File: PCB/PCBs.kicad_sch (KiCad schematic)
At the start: 1 part, among them U1 ADS1299IPAGR

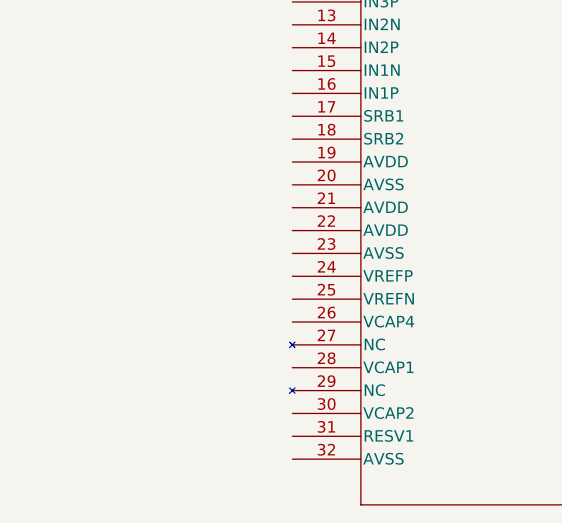
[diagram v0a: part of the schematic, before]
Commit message: adding vcaps
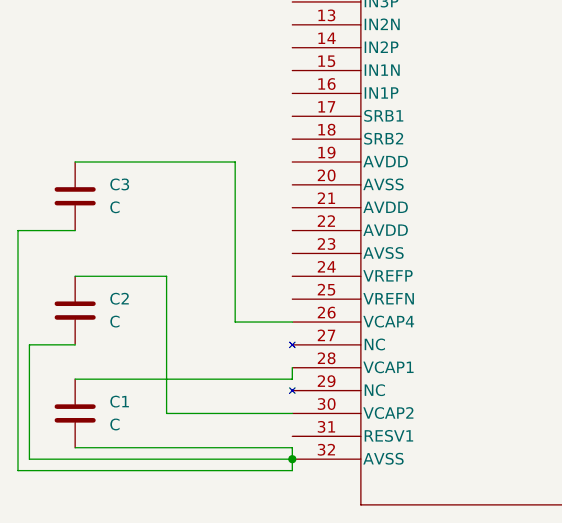
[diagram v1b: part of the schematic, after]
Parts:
- added C1, C2, C3: C, symbol Device:C
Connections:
- net at U1.26 (VCAP4): now also C3.1
- net at U1.28 (VCAP1): now also C1.1
- net at U1.30 (VCAP2): now also C2.1
- net at U1.32 (AVSS): now also C1.2, C2.2, C3.2

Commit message: moving vcaps
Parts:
- added C4: 0.1µF, symbol Device:C
- added C5: 1µF, symbol Device:C
- added U2: ESP32-WROOM-32, ESP32-WROOM-32:MODULE_ESP32-WROOM-32, symbol custom_lib:ESP32-WROOM-32
- C1: value C -> 100µF
- C2, C3: value C -> 1µF
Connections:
- net at U1.26 (VCAP4): now also C5.1; no longer C3.1
- net AVSS: now reaches C1.2, C2.2
- net AVSS: now also C3.1, C4.1, C5.2; no longer C3.2, U1.32 (AVSS)
- net at U1.55 (VCAP3): now also C3.2, C4.2
- new net: U2.1 (GND), U2.15 (GND), U2.38 (GND), U2.39_1 (GND), U2.39_10 (GND), U2.39_11 (GND), U2.39_12 (GND), U2.39_13 (GND), U2.39_14 (GND), U2.39_15 (GND), U2.39_16 (GND), U2.39_17 (GND), U2.39_18 (GND), U2.39_19 (GND), U2.39_2 (GND), U2.39_20 (GND), U2.39_21 (GND), U2.39_3 (GND), U2.39_4 (GND), U2.39_5 (GND), U2.39_6 (GND), U2.39_7 (GND), U2.39_8 (GND), U2.39_9 (GND)

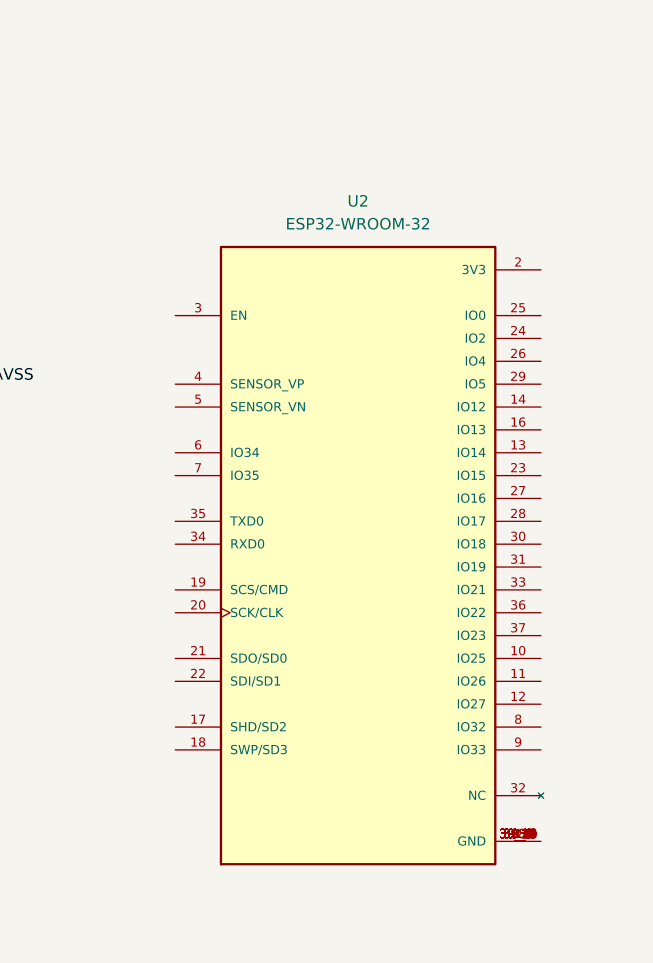
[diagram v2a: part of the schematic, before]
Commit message: esp32 to pi pico
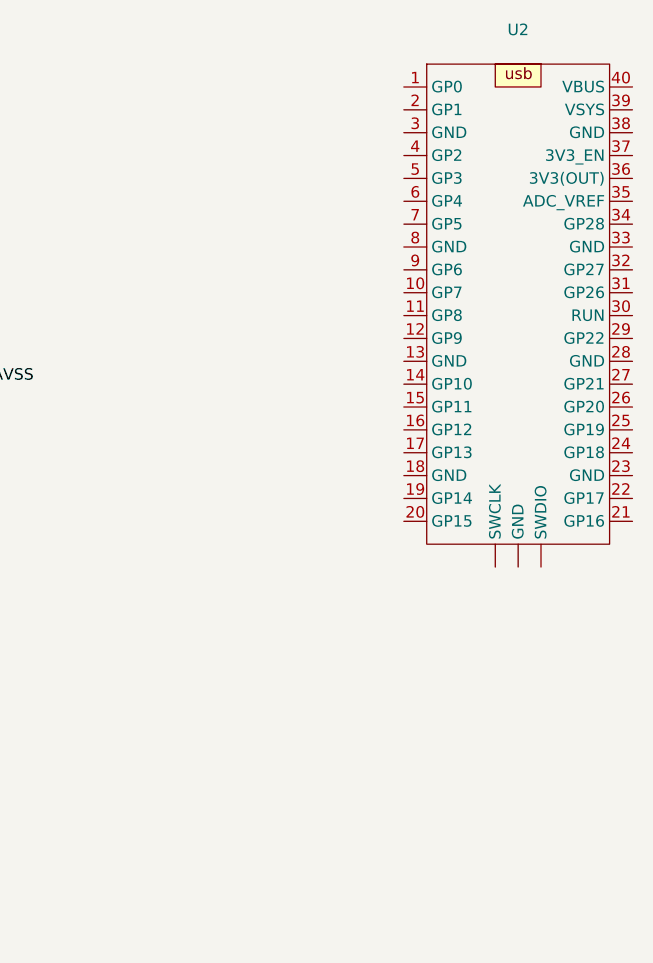
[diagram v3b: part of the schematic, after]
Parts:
- removed U2: ESP32-WROOM-32, ESP32-WROOM-32:MODULE_ESP32-WROOM-32, symbol custom_lib:ESP32-WROOM-32
- added U2: ~, Library:Raspberry_pi_pico, symbol custom_lib:pi_pico
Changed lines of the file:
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@@
 	)
 	(symbol
-		(lib_id "custom_lib:ESP32-WROOM-32")
-		(at 251.46 104.14 0)
+		(lib_id "custom_lib:pi_pico")
+		(at 269.24 45.72 0)
 		(unit 1)
 		(exclude_from_sim no)
@@
 		(fields_autoplaced yes)
 		(property "Reference" "U2"
-			(at 251.46 63.5 0)
+			(at 269.24 44.45 0)
 			(effects
 				(font
@@
 			)
 		)
-		(property "Value" "ESP32-WROOM-32"
-			(at 251.46 66.04 0)
+		(property "Value" "~"
+			(at 269.24 46.99 0)
 			(effects
 				(font
@@
 			)
 		)
-		(property "Footprint" "ESP32-WROOM-32:MODULE_ESP32-WROOM-32"
-			(at 251.46 104.14 0)
+		(property "Footprint" "Library:Raspberry_pi_pico"
+			(at 269.24 45.72 0)
 			(effects
 				(font
 					(size 1.27 1.27)
 				)
-				(justify bottom)
 				(hide yes)
 			)
 		)
 		(property "Datasheet" ""
-			(at 251.46 104.14 0)
+			(at 269.24 45.72 0)
 			(effects
 				(font
@@
 		)
 		(property "Description" ""
-			(at 251.46 104.14 0)
+			(at 269.24 45.72 0)
 			(effects
 				(font
@@
 			)
 		)
-		(property "MF" "Espressif Systems"
-			(at 251.46 104.14 0)
-			(effects
-				(font
-					(size 1.27 1.27)
-				)
-				(justify bottom)
-				(hide yes)
-			)
+		(pin "10"
 		)
-		(property "MAXIMUM_PACKAGE_HEIGHT" "3.2 mm"
-			(at 251.46 104.14 0)
-			(effects
-				(font
-					(size 1.27 1.27)
-				)
-				(justify bottom)
-				(hide yes)
-			)
+		(pin "22"
 		)
-		(property "Package" "None"
-			(at 251.46 104.14 0)
-			(effects
-				(font
-					(size 1.27 1.27)
-				)
-				(justify bottom)
-				(hide yes)
-			)
+		(pin "23"
 		)
-		(property "Price" "None"
-			(at 251.46 104.14 0)
-			(effects
-				(font
-					(size 1.27 1.27)
-				)
-				(justify bottom)
-				(hide yes)
-			)
+		(pin "34"
 		)
-		(property "Check_prices" "https://www.snapeda.com/parts/ESP32-WROOM-32/Espressif+Systems/view-part/?ref=eda"
-			(at 251.46 104.14 0)
-			(effects
-				(font
-					(size 1.27 1.27)
-				)
-				(justify bottom)
-				(hide yes)
-			)
+		(pin "26"
 		)
-		(property "STANDARD" "Manufacturer Recommendations"
-			(at 251.46 104.14 0)
-			(effects
-				(font
-					(size 1.27 1.27)
-				)
-				(justify bottom)
-				(hide yes)
-			)
+		(pin "31"
 		)
-		(property "PARTREV" "2.9"
-			(at 251.46 104.14 0)
-			(effects
-				(font
-					(size 1.27 1.27)
-				)
-				(justify bottom)
-				(hide yes)
-			)
+		(pin "20"
 		)
-		(property "SnapEDA_Link" "https://www.snapeda.com/parts/ESP32-WROOM-32/Espressif+Systems/view-part/?ref=snap"
-			(at 251.46 104.14 0)
-			(effects
-				(font
-					(size 1.27 1.27)
-				)
-				(justify bottom)
-				(hide yes)
-			)
+		(pin "16"
 		)
-		(property "MP" "ESP32-WROOM-32"
-			(at 251.46 104.14 0)
-			(effects
-				(font
-					(size 1.27 1.27)
-				)
-				(justify bottom)
-				(hide yes)
-			)
+		(pin "25"
 		)
-		(property "Description_1" "\nBluetooth, WiFi 802.11b/g/n, Bluetooth v4.2 +EDR, Class 1, 2 and 3 Transceiver Module 2.4GHz ~ 2.5GHz Antenna Not Included, U.FL Surface Mount\n"
-			(at 251.46 104.14 0)
-			(effects
-				(font
-					(size 1.27 1.27)
-				)
-				(justify bottom)
-				(hide yes)
-			)
+		(pin "24"
 		)
-		(property "Availability" "In Stock"
-			(at 251.46 104.14 0)
-			(effects
-				(font
-					(size 1.27 1.27)
-				)
-				(justify bottom)
-				(hide yes)
-			)
+		(pin "11"
 		)
-		(property "MANUFACTURER" "Espressif Systems"
-			(at 251.46 104.14 0)
-			(effects
-				(font
-					(size 1.27 1.27)
-				)
-				(justify bottom)
-				(hide yes)
-			)
+		(pin "21"
+		)
+		(pin "27"
+		)
+		(pin "29"
+		)
+		(pin "13"
+		)
+		(pin "14"
+		)
+		(pin "28"
+		)
+		(pin "3"
+		)
+		(pin "19"
+		)
+		(pin "18"
+		)
+		(pin "30"
+		)
+		(pin "32"
+		)
+		(pin "12"
+		)
+		(pin "33"
+		)
+		(pin "17"
+		)
+		(pin "15"
+		)
+		(pin "35"
+		)
+		(pin "39"
+		)
+		(pin "4"
+		)
+		(pin "37"
+		)
+		(pin ""
+		)
+		(pin ""
+		)
+		(pin "6"
 		)
 		(pin "1"
 		)
-		(pin "39_17"
-		)
-		(pin "23"
-		)
-		(pin "39_5"
-		)
-		(pin "22"
-		)
-		(pin "39_6"
-		)
-		(pin "39_3"
-		)
-		(pin "39_7"
-		)
-		(pin "39_8"
-		)
-		(pin "21"
-		)
-		(pin "39_9"
-		)
-		(pin "10"
-		)
-		(pin "13"
-		)
-		(pin "18"
-		)
-		(pin "31"
-		)
-		(pin "39_11"
-		)
-		(pin "12"
-		)
-		(pin "20"
-		)
-		(pin "34"
-		)
-		(pin "14"
-		)
-		(pin "16"
-		)
-		(pin "27"
-		)
-		(pin "32"
-		)
-		(pin "25"
-		)
-		(pin "19"
-		)
-		(pin "39_20"
-		)
-		(pin "30"
-		)
-		(pin "33"
+		(pin "7"
 		)
 		(pin "38"
 		)
-		(pin "39_10"
+		(pin "8"
 		)
-		(pin "39_12"
-		)
-		(pin "39_14"
-		)
-		(pin "2"
-		)
-		(pin "26"
-		)
-		(pin "3"
-		)
-		(pin "39_19"
-		)
-		(pin "39_21"
+		(pin ""
 		)
 		(pin "36"
-		)
-		(pin "39_16"
-		)
-		(pin "39_4"
-		)
-		(pin "17"
-		)
-		(pin "29"
-		)
-		(pin "28"
-		)
-		(pin "35"
-		)
-		(pin "11"
-		)
-		(pin "24"
-		)
-		(pin "37"
-		)
-		(pin "15"
-		)
-		(pin "39_1"
-		)
-		(pin "39_13"
-		)
-		(pin "39_15"
-		)
-		(pin "39_18"
-		)
-		(pin "39_2"
-		)
-		(pin "4"
 		)
 		(pin "5"
@@
 		(pin "9"
 		)
-		(pin "6"
+		(pin "40"
 		)
-		(pin "8"
-		)
-		(pin "7"
+		(pin "2"
 		)
 		(instances

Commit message: vref pins
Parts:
- added C6: 10µF, symbol Device:C
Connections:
- net AVSS: now also U1.25 (VREFN), C6.2
- net at U1.24 (VREFP): now also C6.1
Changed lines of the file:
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@@
 		(color 0 0 0 0)
 	)
+	(junction
+		(at 95.25 119.38)
+		(diameter 0)
+		(color 0 0 0 0)
+	)
 	(wire
 		(pts
@@
 	(wire
 		(pts
+			(xy 88.9 119.38) (xy 95.25 119.38)
+		)
+		(stroke
+			(width 0)
+			(type default)
+		)
+	)
+	(wire
+		(pts
 			(xy 91.44 137.16) (xy 95.25 137.16)
 		)
@@
 	(wire
 		(pts
+			(xy 95.25 119.38) (xy 95.25 123.19)
+		)
+		(stroke
+			(width 0)
+			(type default)
+		)
+	)
+	(wire
+		(pts
 			(xy 205.74 87.63) (xy 205.74 83.82)
 		)
@@
 	(wire
 		(pts
+			(xy 102.87 119.38) (xy 104.14 119.38)
+		)
+		(stroke
+			(width 0)
+			(type default)
+		)
+	)
+	(wire
+		(pts
 			(xy 102.87 130.81) (xy 111.76 130.81)
 		)
@@
 	(wire
 		(pts
+			(xy 104.14 120.65) (xy 111.76 120.65)
+		)
+		(stroke
+			(width 0)
+			(type default)
+		)
+	)
+	(wire
+		(pts
 			(xy 107.95 125.73) (xy 107.95 143.51)
 		)
@@
 	(wire
 		(pts
+			(xy 95.25 123.19) (xy 111.76 123.19)
+		)
+		(stroke
+			(width 0)
+			(type default)
+		)
+	)
+	(wire
+		(pts
 			(xy 91.44 143.51) (xy 91.44 137.16)
+		)
+		(stroke
+			(width 0)
+			(type default)
+		)
+	)
+	(wire
+		(pts
+			(xy 104.14 119.38) (xy 104.14 120.65)
 		)
 		(stroke
@@
 	(label "AVSS"
 		(at 210.82 83.82 0)
+		(fields_autoplaced yes)
+		(effects
+			(font
+				(size 1.27 1.27)
+			)
+			(justify left bottom)
+		)
+	)
+	(label "AVSS"
+		(at 88.9 119.38 0)
 		(fields_autoplaced yes)
 		(effects
@@
 					(unit 1)
 				)
+			)
+		)
+	)
+	(symbol
+		(lib_id "Device:C")
+		(at 99.06 119.38 270)
+		(unit 1)
+		(exclude_from_sim no)
+		(in_bom yes)
+		(on_board yes)
+		(dnp no)
+		(property "Reference" "C6"
+			(at 103.886 114.3 90)
+			(effects
+				(font
+					(size 1.27 1.27)
+				)
+			)
+		)
+		(property "Value" "10µF "
+			(at 103.886 116.84 90)
+			(effects
+				(font
+					(size 1.27 1.27)
+				)
+			)
+		)
+		(property "Footprint" ""
+			(at 95.25 120.3452 0)
+			(effects
+				(font
+					(size 1.27 1.27)
+				)
+				(hide yes)
+			)
+		)
+		(property "Datasheet" "~"
+			(at 99.06 119.38 0)
+			(effects
+				(font
+					(size 1.27 1.27)
+				)
+				(hide yes)
+			)
+		)
+		(property "Description" "Unpolarized capacitor"
+			(at 99.06 119.38 0)
+			(effects
+				(font
+					(size 1.27 1.27)
+				)
+				(hide yes)
+			)
+		)
+		(pin "1"
+		)
+		(pin "2"
+		)
+		(instances
+			(project "PCBs"
+				(path "/5beccadf-d27e-4f5e-8faf-404ef06d8def"
+					(reference "C6")
+					(unit 1)
+				)

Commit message: ads1299 symbol planning
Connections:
- net at U1.19 (AVDD): now also U1.21 (AVDD), U1.22 (AVDD)
- net at U1.54 (AVDD1): now also U1.56 (AVDD), U1.59 (AVDD)
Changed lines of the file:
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@@
+	)
+	(junction
+		(at 111.76 113.03)
+		(diameter 0)
+		(color 0 0 0 0)
 	)
 	(junction
@@
 		(color 0 0 0 0)
 	)
+	(junction
+		(at 185.42 82.55)
+		(diameter 0)
+		(color 0 0 0 0)
+	)
 	(wire
 		(pts
@@
 	(wire
 		(pts
+			(xy 111.76 113.03) (xy 111.76 115.57)
+		)
+		(stroke
+			(width 0)
+			(type default)
+		)
+	)
+	(wire
+		(pts
 			(xy 205.74 83.82) (xy 205.74 81.28)
 		)
@@
 	(wire
 		(pts
+			(xy 109.22 107.95) (xy 109.22 113.03)
+		)
+		(stroke
+			(width 0)
+			(type default)
+		)
+	)
+	(wire
+		(pts
 			(xy 88.9 119.38) (xy 95.25 119.38)
 		)
@@
 	(wire
 		(pts
+			(xy 111.76 107.95) (xy 109.22 107.95)
+		)
+		(stroke
+			(width 0)
+			(type default)
+		)
+	)
+	(wire
+		(pts
+			(xy 182.88 74.93) (xy 185.42 74.93)
+		)
+		(stroke
+			(width 0)
+			(type default)
+		)
+	)
+	(wire
+		(pts
 			(xy 199.39 81.28) (xy 205.74 81.28)
 		)
@@
 	(wire
 		(pts
+			(xy 185.42 82.55) (xy 185.42 87.63)
+		)
+		(stroke
+			(width 0)
+			(type default)
+		)
+	)
+	(wire
+		(pts
 			(xy 95.25 119.38) (xy 95.25 123.19)
 		)
@@
 	(wire
 		(pts
+			(xy 182.88 82.55) (xy 185.42 82.55)
+		)
+		(stroke
+			(width 0)
+			(type default)
+		)
+	)
+	(wire
+		(pts
 			(xy 102.87 130.81) (xy 111.76 130.81)
 		)
@@
 	(wire
 		(pts
+			(xy 109.22 113.03) (xy 111.76 113.03)
+		)
+		(stroke
+			(width 0)
+			(type default)
+		)
+	)
+	(wire
+		(pts
 			(xy 91.44 143.51) (xy 91.44 137.16)
 		)
@@
 	(wire
 		(pts
+			(xy 182.88 87.63) (xy 185.42 87.63)
+		)
+		(stroke
+			(width 0)
+			(type default)
+		)
+	)
+	(wire
+		(pts
 			(xy 111.76 135.89) (xy 106.68 135.89)
 		)
 		(stroke
+			(width 0)
+			(type default)
+		)
+	)
+	(wire
+		(pts
+			(xy 185.42 74.93) (xy 185.42 82.55)
+		)
+		(stroke

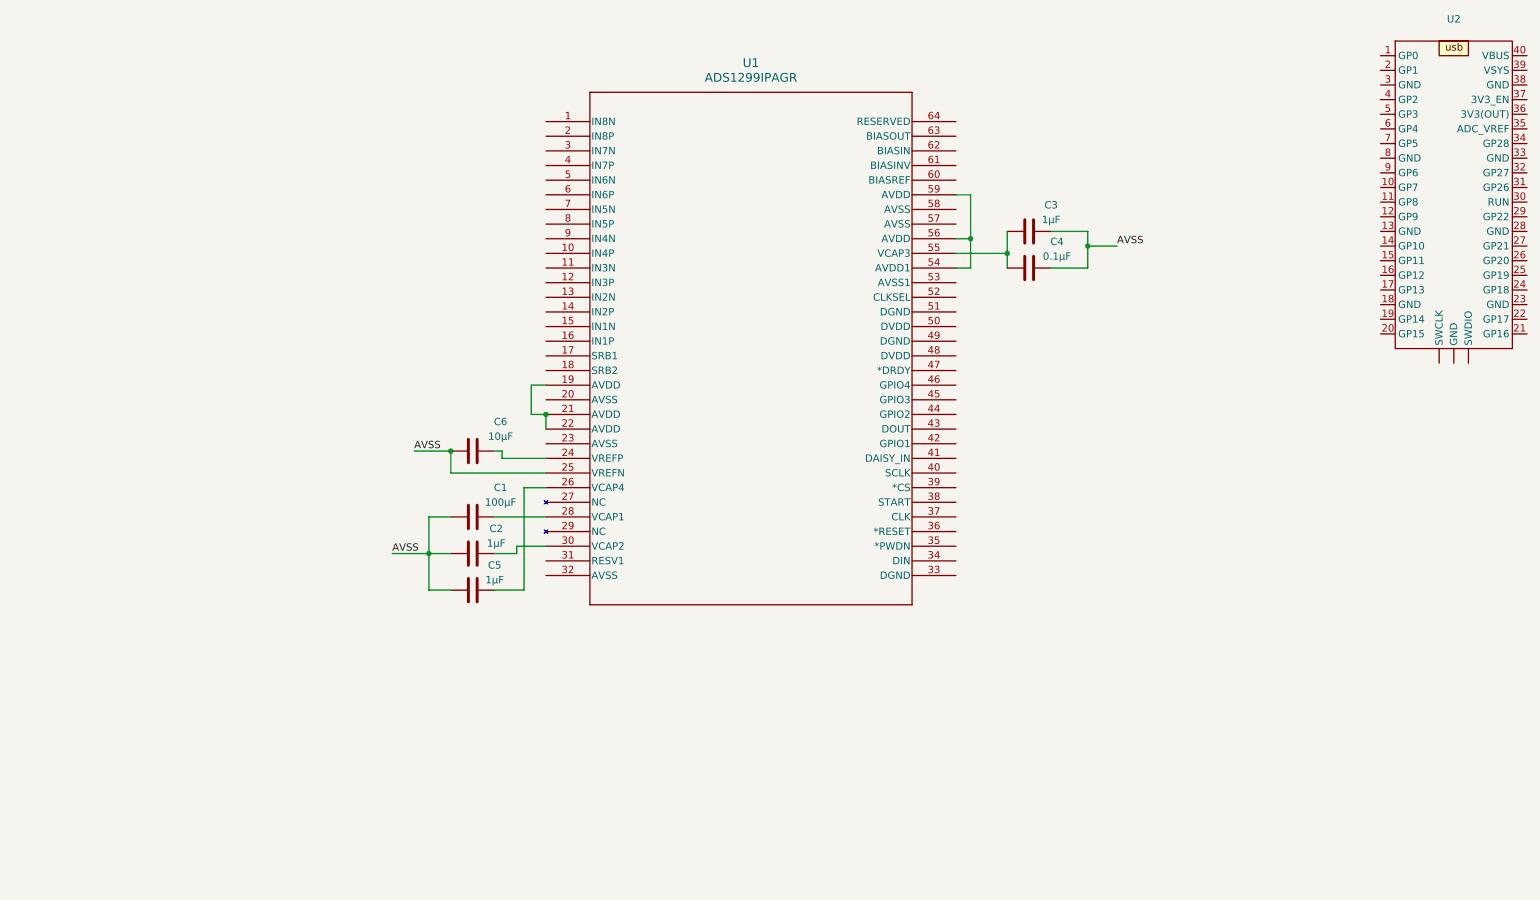
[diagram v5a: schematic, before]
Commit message: ads1299 final symbol plan
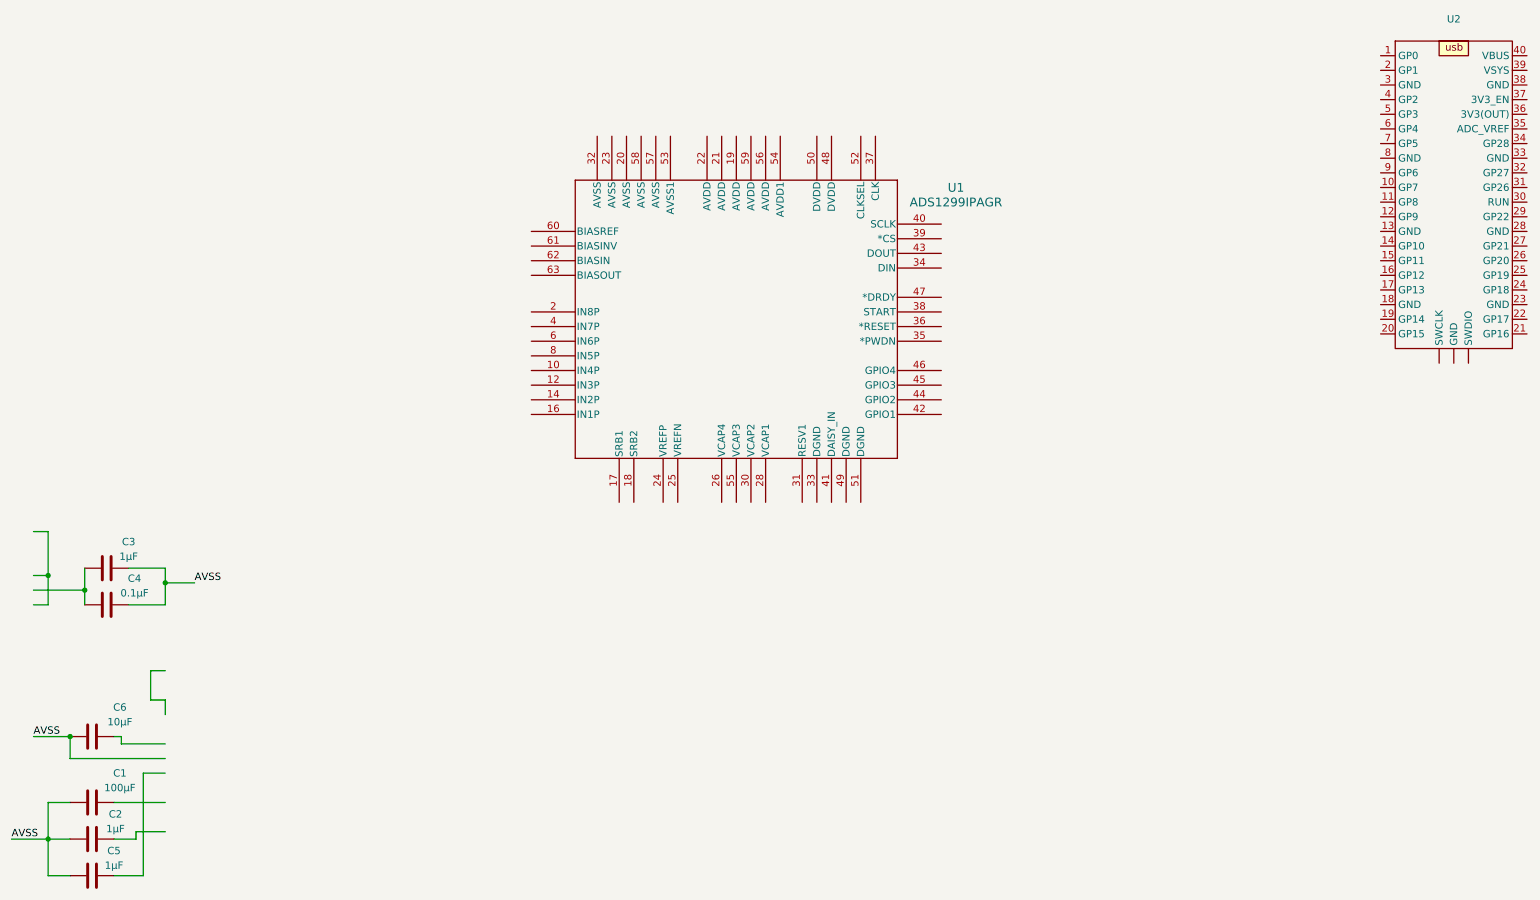
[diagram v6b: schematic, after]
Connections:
- net AVSS: no longer U1.25 (VREFN)
- net at C5.1: no longer U1.26 (VCAP4)
- net at C1.1: no longer U1.28 (VCAP1)
- net at C3.2, C4.2: no longer U1.55 (VCAP3)
- net at C2.1: no longer U1.30 (VCAP2)
- net at U1.24 (VREFP): no longer C6.1
- now unconnected: U1.19 (AVDD), U1.21 (AVDD), U1.22 (AVDD), U1.54 (AVDD1), U1.56 (AVDD), U1.59 (AVDD)
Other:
- moved on the sheet: C1, C2, C3, C4, C5, C6
